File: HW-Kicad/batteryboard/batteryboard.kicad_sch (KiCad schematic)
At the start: 9 parts, among them J1 Conn_01x05_Male, J2 Conn_01x01_Male, J3 Conn_01x01_Male, J4 Conn_01x01_Male, J5 Conn_01x01_Male, J6 Conn_01x01_Male, J7 Conn_01x02_Male, U1 YAAJ_DCDC_StepDown_LM2596

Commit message: version final de la batery board
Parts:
- J7: footprint Connector_Molex:Molex_KK-254_AE-6410-02A_1x02_P2.54mm_Vertical -> Connector_Molex:Molex_KK-254_AE-6410-03A_1x03_P2.54mm_Vertical; symbol Connector:Conn_01x02_Male -> Connector:Conn_01x03_Male
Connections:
- net at F1.2, U1.1 (Vin): now also J7.3 (Pin_3)
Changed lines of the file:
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@@
   (junction (at 52.07 55.88) (diameter 0) (color 0 0 0 0)
   )
+  (junction (at 133.35 53.34) (diameter 0) (color 0 0 0 0)
+  )
   (junction (at 142.24 63.5) (diameter 0) (color 0 0 0 0)
   )
   (junction (at 85.09 54.61) (diameter 0) (color 0 0 0 0)
   )
-  (wire (pts (xy 176.53 53.34) (xy 176.53 58.42))
-    (stroke (width 0) (type default) (color 0 0 0 0))
-  )
   (wire (pts (xy 52.07 53.34) (xy 52.07 55.88))
     (stroke (width 0) (type default) (color 0 0 0 0))
@@
     (stroke (width 0) (type default) (color 0 0 0 0))
   )
+  (wire (pts (xy 133.35 53.34) (xy 134.62 53.34))
+    (stroke (width 0) (type default) (color 0 0 0 0))
+  )
   (wire (pts (xy 85.09 54.61) (xy 85.09 59.69))
     (stroke (width 0) (type default) (color 0 0 0 0))
@@
     (stroke (width 0) (type default) (color 0 0 0 0))
   )
+  (wire (pts (xy 176.53 55.88) (xy 163.83 55.88))
+    (stroke (width 0) (type default) (color 0 0 0 0))
+  )
+  (wire (pts (xy 179.07 74.93) (xy 133.35 74.93))
+    (stroke (width 0) (type default) (color 0 0 0 0))
+  )
   (wire (pts (xy 147.32 63.5) (xy 142.24 63.5))
     (stroke (width 0) (type default) (color 0 0 0 0))
   )
+  (wire (pts (xy 176.53 53.34) (xy 176.53 55.88))
+    (stroke (width 0) (type default) (color 0 0 0 0))
+  )
   (wire (pts (xy 59.69 55.88) (xy 59.69 59.69))
     (stroke (width 0) (type default) (color 0 0 0 0))
@@
     (stroke (width 0) (type default) (color 0 0 0 0))
   )
-  (wire (pts (xy 154.94 53.34) (xy 173.99 53.34))
-    (stroke (width 0) (type default) (color 0 0 0 0))
-  )
-  (wire (pts (xy 132.08 53.34) (xy 134.62 53.34))
+  (wire (pts (xy 133.35 74.93) (xy 133.35 53.34))
+    (stroke (width 0) (type default) (color 0 0 0 0))
+  )
+  (wire (pts (xy 163.83 55.88) (xy 163.83 53.34))
+    (stroke (width 0) (type default) (color 0 0 0 0))
+  )
+  (wire (pts (xy 132.08 53.34) (xy 133.35 53.34))
     (stroke (width 0) (type default) (color 0 0 0 0))
   )
@@
     (stroke (width 0) (type default) (color 0 0 0 0))
   )
+  (wire (pts (xy 173.99 53.34) (xy 173.99 59.69))
+    (stroke (width 0) (type default) (color 0 0 0 0))
+  )
   (wire (pts (xy 52.07 55.88) (xy 52.07 59.69))
     (stroke (width 0) (type default) (color 0 0 0 0))
   )
+  (wire (pts (xy 163.83 53.34) (xy 154.94 53.34))
+    (stroke (width 0) (type default) (color 0 0 0 0))
+  )
+  (wire (pts (xy 85.09 53.34) (xy 124.46 53.34))
+    (stroke (width 0) (type default) (color 0 0 0 0))
+  )
   (wire (pts (xy 45.72 55.88) (xy 52.07 55.88))
     (stroke (width 0) (type default) (color 0 0 0 0))
@@
     (stroke (width 0) (type default) (color 0 0 0 0))
   )
-  (wire (pts (xy 124.46 53.34) (xy 85.09 53.34))
+  (wire (pts (xy 179.07 53.34) (xy 179.07 74.93))
     (stroke (width 0) (type default) (color 0 0 0 0))
   )
@@
     (pin "1")
   )
-  (symbol (lib_id "Connector:Conn_01x02_Male") (at 176.53 48.26 270) (unit 1)
-    (in_bom yes) (on_board yes) (fields_autoplaced)
-    (property "Reference" "J7" (id 0) (at 177.8 47.6249 90)
-      (effects (font (size 1.27 1.27)) (justify left))
-    )
-    (property "Value" "Conn_01x02_Male" (id 1) (at 177.8 50.1649 90)
-      (effects (font (size 1.27 1.27)) (justify left))
-    )
-    (property "Footprint" "Connector_Molex:Molex_KK-254_AE-6410-02A_1x02_P2.54mm_Vertical" (id 2) (at 176.53 48.26 0)
+  (symbol (lib_id "Connector:Conn_01x03_Male") (at 176.53 48.26 90) (mirror x) (unit 1)
+    (in_bom yes) (on_board yes) (fields_autoplaced)
+    (property "Reference" "J7" (id 0) (at 176.53 43.18 90))
+    (property "Value" "Conn_01x02_Male" (id 1) (at 176.53 45.72 90))
+    (property "Footprint" "Connector_Molex:Molex_KK-254_AE-6410-03A_1x03_P2.54mm_Vertical" (id 2) (at 176.53 48.26 0)
       (effects (font (size 1.27 1.27)) hide)
     )
@@
     (pin "1")
     (pin "2")
-  )
-  (symbol (lib_id "power:GND") (at 176.53 58.42 0) (unit 1)
-    (in_bom yes) (on_board yes) (fields_autoplaced)
-    (property "Reference" "#PWR0103" (id 0) (at 176.53 64.77 0)
-      (effects (font (size 1.27 1.27)) hide)
-    )
-    (property "Value" "GND" (id 1) (at 176.53 63.5 0))
-    (property "Footprint" "" (id 2) (at 176.53 58.42 0)
-      (effects (font (size 1.27 1.27)) hide)
-    )
-    (property "Datasheet" "" (id 3) (at 176.53 58.42 0)
+    (pin "3")
+  )
+  (symbol (lib_id "power:GND") (at 173.99 59.69 0) (unit 1)
+    (in_bom yes) (on_board yes) (fields_autoplaced)
+    (property "Reference" "#PWR0103" (id 0) (at 173.99 66.04 0)
+      (effects (font (size 1.27 1.27)) hide)
+    )
+    (property "Value" "GND" (id 1) (at 173.99 64.77 0))
+    (property "Footprint" "" (id 2) (at 173.99 59.69 0)
+      (effects (font (size 1.27 1.27)) hide)
+    )
+    (property "Datasheet" "" (id 3) (at 173.99 59.69 0)
       (effects (font (size 1.27 1.27)) hide)
     )
@@
     )
     (path "/bef7d675-bafd-490e-992c-092fb3e6883e"
-      (reference "J7") (unit 1) (value "Conn_01x02_Male") (footprint "Connector_Molex:Molex_KK-254_AE-6410-02A_1x02_P2.54mm_Vertical")
+      (reference "J7") (unit 1) (value "Conn_01x02_Male") (footprint "Connector_Molex:Molex_KK-254_AE-6410-03A_1x03_P2.54mm_Vertical")
     )
     (path "/646819fa-ebcd-49a0-86bb-5a5a8ea6ca08"

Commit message: version final de placa baterías
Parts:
- removed U1: YAAJ_DCDC_StepDown_LM2596, LM2596:YAAJ_DCDC_StepDown_LM2596, symbol LM2596:YAAJ_DCDC_StepDown_LM2596
- added F2: Fuse, Fuse:Fuseholder_Blade_Mini_Keystone_3568, symbol Device:Fuse
- added J8, J9: Conn_01x02_Male, TerminalBlock:TerminalBlock_bornier-2_P5.08mm, symbol Connector:Conn_01x02_Male
- added Q1, Q2: ATP213, Package_TO_SOT_SMD:TO-252-2, symbol Transistor_FET:STD7NK40Z
- added R1, R3: 10k, Resistor_THT:R_Axial_DIN0207_L6.3mm_D2.5mm_P10.16mm_Horizontal, symbol Device:R
- added R2, R4: 100k, Resistor_THT:R_Axial_DIN0207_L6.3mm_D2.5mm_P10.16mm_Horizontal, symbol Device:R
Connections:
- net GND: now also J7.3 (Pin_3), Q1.3 (S), Q2.3 (S), R2.1, R4.1; no longer J7.1 (Pin_1)
- net at F1.1, J1.1 (Pin_1), J6.1 (Pin_1): now also F2.1
- net at F1.2: now also J7.1 (Pin_1); no longer J7.3 (Pin_3)
- net abortSig: now reaches J7.2 (Pin_2)
- net abortSig: now also R1.1, R3.1
- new net: Q2.1 (G), R3.2, R4.2
- new net: F2.2, J8.2 (Pin_2), J9.2 (Pin_2)
- new net: J8.1 (Pin_1), Q1.2 (D)
- new net: Q1.1 (G), R1.2, R2.2
- new net: J9.1 (Pin_1), Q2.2 (D)
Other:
- moved on the sheet: J7

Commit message: cambie para tener dos señales de  control distintas
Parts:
- J7: value Conn_01x02_Male -> Conn_01x04_Male; footprint Connector_Molex:Molex_KK-254_AE-6410-03A_1x03_P2.54mm_Vertical -> Connector_Molex:Molex_KK-254_AE-6410-04A_1x04_P2.54mm_Vertical; symbol Connector:Conn_01x03_Male -> Connector:Conn_01x04_Male
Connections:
- net GND: now also J7.4 (Pin_4); no longer J7.3 (Pin_3)
- net abortSig: no longer R3.1
- new net parachuteSIG: J7.3 (Pin_3), R3.1
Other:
- moved on the sheet: J9, Q2, R3, R4

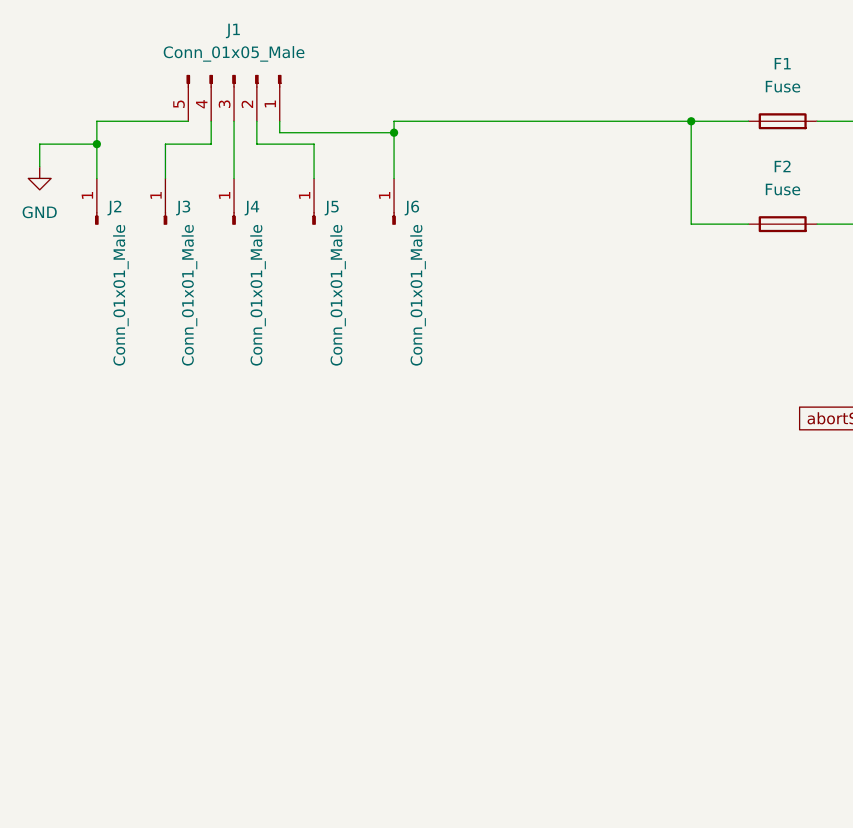
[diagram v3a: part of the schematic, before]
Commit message: agregue pines de baterías para aprs
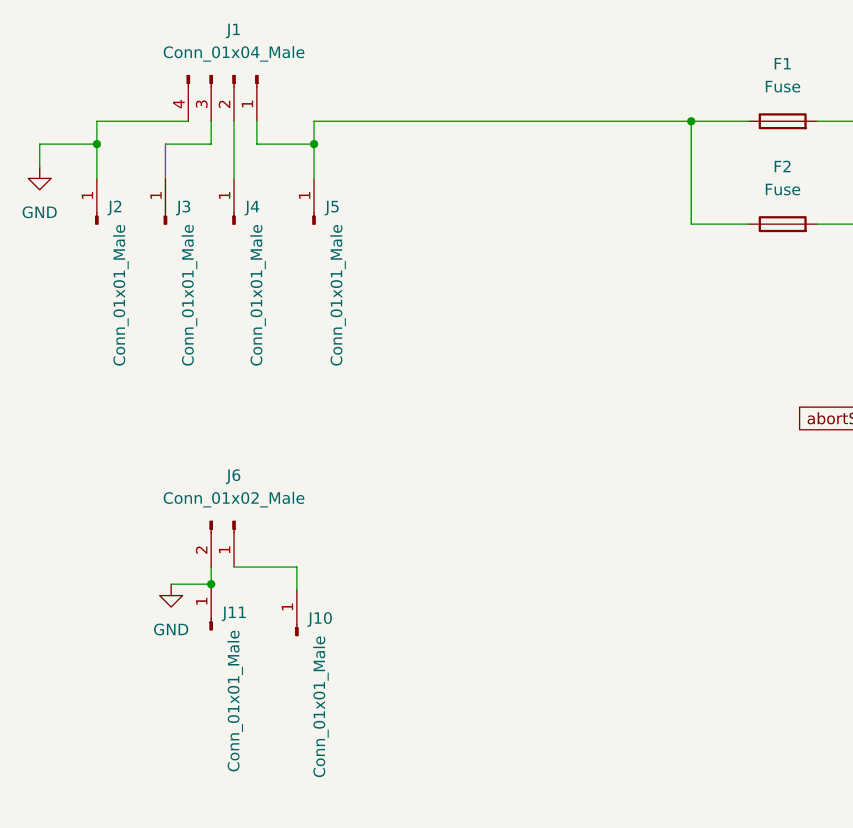
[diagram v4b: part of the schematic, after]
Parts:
- removed J6: Conn_01x01_Male, Connector_PinHeader_2.54mm:PinHeader_1x01_P2.54mm_Vertical, symbol Connector:Conn_01x01_Male
- added J10, J11: Conn_01x01_Male, Connector_PinHeader_2.54mm:PinHeader_1x01_P2.54mm_Vertical, symbol Connector:Conn_01x01_Male
- added J6: Conn_01x02_Male, Connector_Molex:Molex_KK-254_AE-6410-02A_1x02_P2.54mm_Vertical, symbol Connector:Conn_01x02_Male
- J1: value Conn_01x05_Male -> Conn_01x04_Male; footprint Connector_Molex:Molex_KK-254_AE-6410-05A_1x05_P2.54mm_Vertical -> Connector_Molex:Molex_KK-254_AE-6410-04A_1x04_P2.54mm_Vertical; symbol Connector:Conn_01x05_Male -> Connector:Conn_01x04_Male
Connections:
- net GND: now also J1.4 (Pin_4), J11.1 (Pin_1), J6.2 (Pin_2); no longer J1.5 (Pin_5)
- net at F1.1, F2.1, J1.1 (Pin_1): now also J5.1 (Pin_1)
- net at J1.2 (Pin_2): now also J4.1 (Pin_1); no longer J5.1 (Pin_1)
- net at J3.1 (Pin_1): now also J1.3 (Pin_3); no longer J1.4 (Pin_4)
- new net: J10.1 (Pin_1), J6.1 (Pin_1)
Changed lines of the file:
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@@
   (junction (at 118.11 53.34) (diameter 0) (color 0 0 0 0)
   )
+  (junction (at 64.77 104.775) (diameter 0) (color 0 0 0 0)
+  )
   (junction (at 157.48 96.52) (diameter 0) (color 0 0 0 0)
   )
@@
   (junction (at 157.48 64.77) (diameter 0) (color 0 0 0 0)
   )
+  (junction (at 76.2 55.88) (diameter 0) (color 0 0 0 0)
+  )
   (junction (at 214.63 86.995) (diameter 0) (color 0 0 0 0)
   )
   (junction (at 223.52 97.155) (diameter 0) (color 0 0 0 0)
   )
-  (junction (at 85.09 54.61) (diameter 0) (color 0 0 0 0)
-  )
   (wire (pts (xy 148.59 96.52) (xy 157.48 96.52))
     (stroke (width 0) (type default) (color 0 0 0 0))
   )
+  (wire (pts (xy 76.2 53.34) (xy 76.2 55.88))
+    (stroke (width 0) (type default) (color 0 0 0 0))
+  )
   (wire (pts (xy 157.48 96.52) (xy 157.48 91.44))
     (stroke (width 0) (type default) (color 0 0 0 0))
@@
     (stroke (width 0) (type default) (color 0 0 0 0))
   )
-  (wire (pts (xy 85.09 53.34) (xy 85.09 54.61))
-    (stroke (width 0) (type default) (color 0 0 0 0))
-  )
   (wire (pts (xy 69.85 53.34) (xy 69.85 55.88))
     (stroke (width 0) (type default) (color 0 0 0 0))
@@
     (stroke (width 0) (type default) (color 0 0 0 0))
   )
-  (wire (pts (xy 85.09 54.61) (xy 85.09 59.69))
+  (wire (pts (xy 60.325 104.775) (xy 64.77 104.775))
     (stroke (width 0) (type default) (color 0 0 0 0))
   )
@@
     (stroke (width 0) (type default) (color 0 0 0 0))
   )
+  (wire (pts (xy 74.295 102.87) (xy 74.295 105.41))
+    (stroke (width 0) (type default) (color 0 0 0 0))
+  )
   (wire (pts (xy 132.08 53.34) (xy 147.32 53.34))
     (stroke (width 0) (type default) (color 0 0 0 0))
@@
     (stroke (width 0) (type default) (color 0 0 0 0))
   )
-  (wire (pts (xy 72.39 54.61) (xy 85.09 54.61))
-    (stroke (width 0) (type default) (color 0 0 0 0))
-  )
   (wire (pts (xy 214.63 97.155) (xy 223.52 97.155))
     (stroke (width 0) (type default) (color 0 0 0 0))
@@
     (stroke (width 0) (type default) (color 0 0 0 0))
   )
+  (wire (pts (xy 64.77 104.775) (xy 64.77 102.87))
+    (stroke (width 0) (type default) (color 0 0 0 0))
+  )
   (wire (pts (xy 52.07 55.88) (xy 52.07 59.69))
     (stroke (width 0) (type default) (color 0 0 0 0))
   )
-  (wire (pts (xy 85.09 53.34) (xy 118.11 53.34))
+  (wire (pts (xy 76.2 53.34) (xy 118.11 53.34))
     (stroke (width 0) (type default) (color 0 0 0 0))
   )
@@
     (stroke (width 0) (type default) (color 0 0 0 0))
   )
-  (wire (pts (xy 72.39 53.34) (xy 72.39 54.61))
+  (wire (pts (xy 67.31 102.87) (xy 74.295 102.87))
     (stroke (width 0) (type default) (color 0 0 0 0))
   )
@@
     (pin "1")
   )
-  (symbol (lib_id "Connector:Conn_01x01_Male") (at 85.09 64.77 90) (unit 1)
-    (in_bom yes) (on_board yes)
-    (property "Reference" "J6" (id 0) (at 86.36 62.8649 90)
-      (effects (font (size 1.27 1.27)) (justify right))
-    )
-    (property "Value" "Conn_01x01_Male" (id 1) (at 87.63 64.77 0)
-      (effects (font (size 1.27 1.27)) (justify right))
-    )
-    (property "Footprint" "Connector_PinHeader_2.54mm:PinHeader_1x01_P2.54mm_Vertical" (id 2) (at 85.09 64.77 0)
-      (effects (font (size 1.27 1.27)) hide)
-    )
-    (property "Datasheet" "~" (id 3) (at 85.09 64.77 0)
-      (effects (font (size 1.27 1.27)) hide)
-    )
-    (pin "1")
-  )
   (symbol (lib_id "Device:R") (at 214.63 93.345 180) (unit 1)
     (in_bom yes) (on_board yes) (fields_autoplaced)
@@
     (pin "1")
   )
+  (symbol (lib_id "Connector:Conn_01x01_Male") (at 64.77 109.855 90) (unit 1)
+    (in_bom yes) (on_board yes)
+    (property "Reference" "J11" (id 0) (at 66.04 107.9499 90)
+      (effects (font (size 1.27 1.27)) (justify right))
+    )
+    (property "Value" "Conn_01x01_Male" (id 1) (at 67.31 109.855 0)
+      (effects (font (size 1.27 1.27)) (justify right))
+    )
+    (property "Footprint" "Connector_PinHeader_2.54mm:PinHeader_1x01_P2.54mm_Vertical" (id 2) (at 64.77 109.855 0)
+      (effects (font (size 1.27 1.27)) hide)
+    )
+    (property "Datasheet" "~" (id 3) (at 64.77 109.855 0)
+      (effects (font (size 1.27 1.27)) hide)
+    )
+    (pin "1")
+  )
   (symbol (lib_id "Device:Fuse") (at 128.27 64.77 90) (unit 1)
     (in_bom yes) (on_board yes) (fields_autoplaced)
@@
     (pin "3")
   )
+  (symbol (lib_id "power:GND") (at 60.325 104.775 0) (unit 1)
+    (in_bom yes) (on_board yes) (fields_autoplaced)
+    (property "Reference" "#PWR0105" (id 0) (at 60.325 111.125 0)
+      (effects (font (size 1.27 1.27)) hide)
+    )
+    (property "Value" "GND" (id 1) (at 60.325 109.855 0))
+    (property "Footprint" "" (id 2) (at 60.325 104.775 0)
+      (effects (font (size 1.27 1.27)) hide)
+    )
+    (property "Datasheet" "" (id 3) (at 60.325 104.775 0)
+      (effects (font (size 1.27 1.27)) hide)
+    )
+    (pin "1")
+  )
   (symbol (lib_id "Connector:Conn_01x02_Male") (at 228.6 81.915 180) (unit 1)
     (in_bom yes) (on_board yes)
@@
     (pin "1")
   )
-  (symbol (lib_id "Connector:Conn_01x05_Male") (at 67.31 48.26 270) (unit 1)
+  (symbol (lib_id "Connector:Conn_01x04_Male") (at 67.31 48.26 270) (unit 1)
     (in_bom yes) (on_board yes) (fields_autoplaced)
     (property "Reference" "J1" (id 0) (at 67.31 43.18 90))
-    (property "Value" "Conn_01x05_Male" (id 1) (at 67.31 45.72 90))
-    (property "Footprint" "Connector_Molex:Molex_KK-254_AE-6410-05A_1x05_P2.54mm_Vertical" (id 2) (at 67.31 48.26 0)
+    (property "Value" "Conn_01x04_Male" (id 1) (at 67.31 45.72 90))
+    (property "Footprint" "Connector_Molex:Molex_KK-254_AE-6410-04A_1x04_P2.54mm_Vertical" (id 2) (at 67.31 48.26 0)
       (effects (font (size 1.27 1.27)) hide)
     )
@@
     (pin "3")
     (pin "4")
-    (pin "5")
   )
   (symbol (lib_id "power:GND") (at 45.72 58.42 0) (unit 1)
@@
     )
     (property "Datasheet" "" (id 3) (at 45.72 58.42 0)
+      (effects (font (size 1.27 1.27)) hide)
+    )
+    (pin "1")
+  )
+  (symbol (lib_id "Connector:Conn_01x01_Male") (at 74.295 110.49 90) (unit 1)
+    (in_bom yes) (on_board yes)
+    (property "Reference" "J10" (id 0) (at 75.565 108.5849 90)
+      (effects (font (size 1.27 1.27)) (justify right))
+    )
+    (property "Value" "Conn_01x01_Male" (id 1) (at 76.835 110.49 0)
+      (effects (font (size 1.27 1.27)) (justify right))
+    )
+    (property "Footprint" "Connector_PinHeader_2.54mm:PinHeader_1x01_P2.54mm_Vertical" (id 2) (at 74.295 110.49 0)
+      (effects (font (size 1.27 1.27)) hide)
+    )
+    (property "Datasheet" "~" (id 3) (at 74.295 110.49 0)
       (effects (font (size 1.27 1.27)) hide)
     )
@@
     (pin "3")
   )
+  (symbol (lib_id "Connector:Conn_01x02_Male") (at 67.31 97.79 270) (unit 1)
+    (in_bom yes) (on_board yes) (fields_autoplaced)
+    (property "Reference" "J6" (id 0) (at 67.31 92.71 90))
+    (property "Value" "Conn_01x02_Male" (id 1) (at 67.31 95.25 90))
+    (property "Footprint" "Connector_Molex:Molex_KK-254_AE-6410-02A_1x02_P2.54mm_Vertical" (id 2) (at 67.31 97.79 0)
+      (effects (font (size 1.27 1.27)) hide)
+    )
+    (property "Datasheet" "~" (id 3) (at 67.31 97.79 0)
+      (effects (font (size 1.27 1.27)) hide)
+    )
+    (pin "1")
+    (pin "2")
+  )
   (symbol (lib_id "Connector:Conn_01x01_Male") (at 67.31 64.77 90) (unit 1)
     (in_bom yes) (on_board yes)
@@
       (reference "#PWR0104") (unit 1) (value "GND") (footprint "")
     )
+    (path "/7271ee4d-c6a4-44f6-8d9d-43ba1def025d"
+      (reference "#PWR0105") (unit 1) (value "GND") (footprint "")
+    )
     (path "/26971ca3-43cc-47d7-bf8f-316231e56af3"
       (reference "F1") (unit 1) (value "Fuse") (footprint "Fuse:Fuseholder_Blade_Mini_Keystone_3568")
@@
     )
     (path "/81443754-7db7-44d8-81b1-a140e66ca0f9"
-      (reference "J1") (unit 1) (value "Conn_01x05_Male") (footprint "Connector_Molex:Molex_KK-254_AE-6410-05A_1x05_P2.54mm_Vertical")
+      (reference "J1") (unit 1) (value "Conn_01x04_Male") (footprint "Connector_Molex:Molex_KK-254_AE-6410-04A_1x04_P2.54mm_Vertical")
     )
     (path "/7b68c6fe-f88f-4550-aa2f-d316d0966bfc"
@@
       (reference "J5") (unit 1) (value "Conn_01x01_Male") (footprint "Connector_PinHeader_2.54mm:PinHeader_1x01_P2.54mm_Vertical")
     )
-    (path "/16f80958-e52a-499e-9da6-f4be0da59c42"
-      (reference "J6") (unit 1) (value "Conn_01x01_Male") (footprint "Connector_PinHeader_2.54mm:PinHeader_1x01_P2.54mm_Vertical")
+    (path "/e8c68ab3-5368-417c-a416-c85f71234d8d"
+      (reference "J6") (unit 1) (value "Conn_01x02_Male") (footprint "Connector_Molex:Molex_KK-254_AE-6410-02A_1x02_P2.54mm_Vertical")
     )
     (path "/bef7d675-bafd-490e-992c-092fb3e6883e"
@@
       (reference "J9") (unit 1) (value "Conn_01x02_Male") (footprint "TerminalBlock:TerminalBlock_bornier-2_P5.08mm")
     )
+    (path "/8587668d-a0b0-4271-be9e-1b68dac14e55"
+      (reference "J10") (unit 1) (value "Conn_01x01_Male") (footprint "Connector_PinHeader_2.54mm:PinHeader_1x01_P2.54mm_Vertical")
+    )
+    (path "/3156f698-0dbb-40b2-95f5-7194910fbb91"
+      (reference "J11") (unit 1) (value "Conn_01x01_Male") (footprint "Connector_PinHeader_2.54mm:PinHeader_1x01_P2.54mm_Vertical")
+    )
     (path "/e37f03fd-f568-441f-bf2a-5427ea553ef3"
